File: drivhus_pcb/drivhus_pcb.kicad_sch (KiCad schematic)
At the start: 10 parts, among them J1 Setup, J2 Conn_01x19_Female, J3 Conn_01x19_Female, J4 Conn_01x04_Male, J5 Conn_Coaxial_Power, J6 +12V, J7 -12V, J8 +5V, J9 -5V, U1 SP3485EN

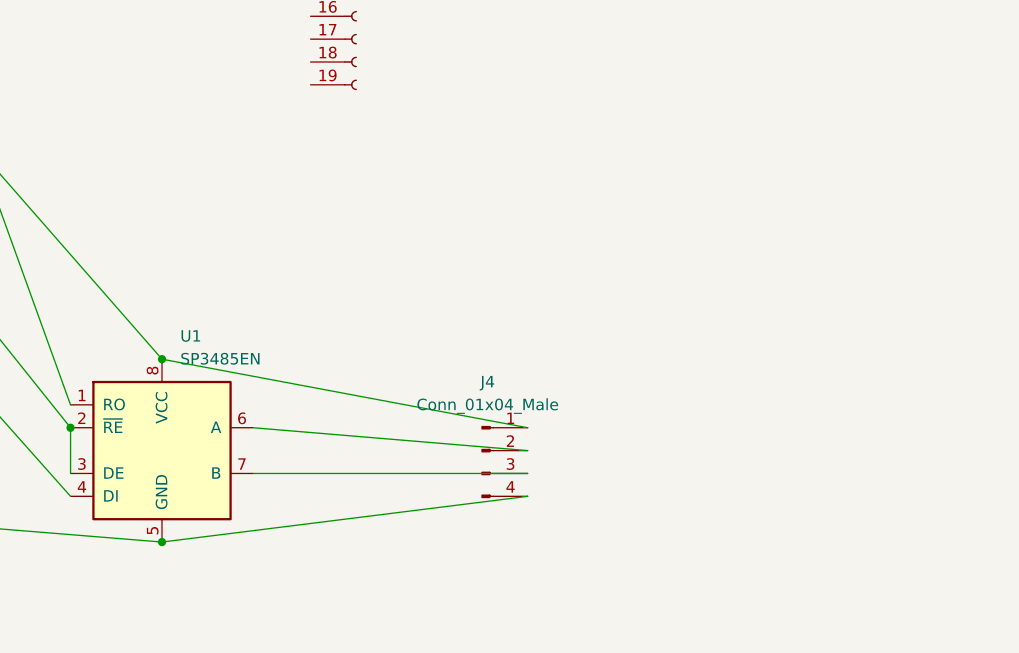
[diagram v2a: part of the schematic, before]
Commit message: Use RJ45 as quick-connect for RS-485 bus. Two connectors, so controller can be in the middle of bus
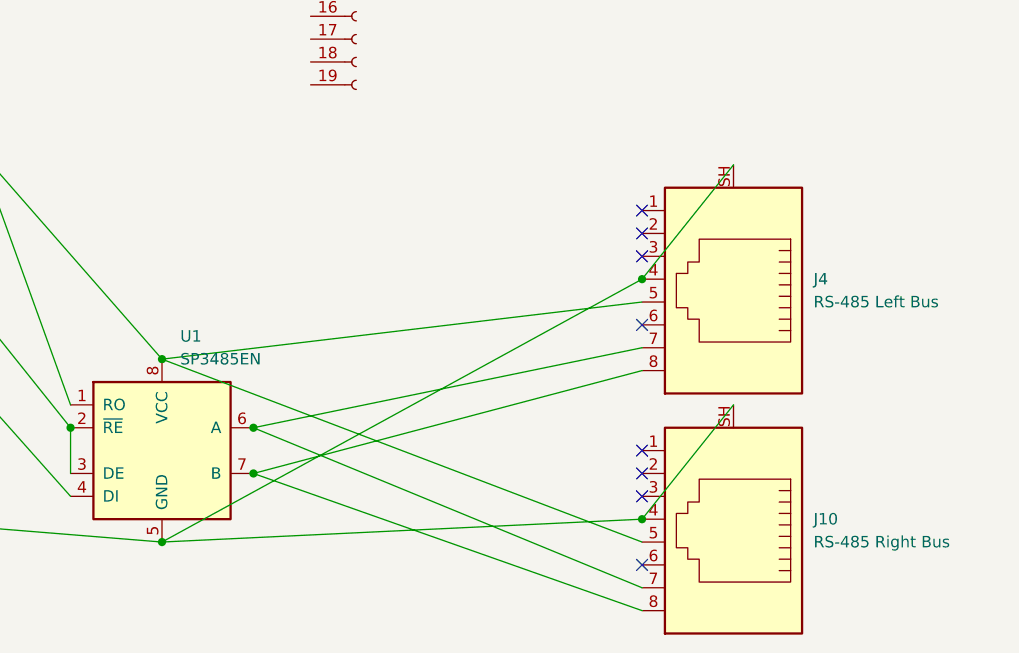
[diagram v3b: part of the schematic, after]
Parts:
- removed J4: Conn_01x04_Male, TerminalBlock:TerminalBlock_bornier-4_P5.08mm, symbol Connector:Conn_01x04_Male
- added J10: RS-485 Right Bus, Connector_RJ:RJ45_Ninigi_GE, symbol Connector:RJ45_Shielded
- added J4: RS-485 Left Bus, Connector_RJ:RJ45_Ninigi_GE, symbol Connector:RJ45_Shielded
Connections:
- net +5V: now also J10.5, J4.5
- net GND: now also J10.4, J10.SH, J4.4, J4.SH
- net at U1.6 (A): now also J10.7, J4.7
- net at U1.7 (B): now also J10.8, J4.8
- no-connect marks 0 -> 8
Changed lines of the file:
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@@
 (kicad_sch (version 20211123) (generator eeschema)
   (paper "A4")
+  (junction (at 179.07 156.21) (diameter 0) (color 0 0 0 0)
+  )
+  (junction (at 68.58 48.26) (diameter 0) (color 0 0 0 0)
+  )
+  (junction (at 44.45 33.02) (diameter 0) (color 0 0 0 0)
+  )
+  (junction (at 44.45 45.72) (diameter 0) (color 0 0 0 0)
+  )
   (junction (at 125.73 158.75) (diameter 0) (color 0 0 0 0)
   )
-  (junction (at 68.58 48.26) (diameter 0) (color 0 0 0 0)
-  )
-  (junction (at 44.45 33.02) (diameter 0) (color 0 0 0 0)
-  )
-  (junction (at 44.45 45.72) (diameter 0) (color 0 0 0 0)
+  (junction (at 135.89 151.13) (diameter 0) (color 0 0 0 0)
+  )
+  (junction (at 179.07 129.54) (diameter 0) (color 0 0 0 0)
   )
   (junction (at 99.06 107.95) (diameter 0) (color 0 0 0 0)
   )
+  (junction (at 135.89 146.05) (diameter 0) (color 0 0 0 0)
+  )
+  (junction (at 68.58 33.02) (diameter 0) (color 0 0 0 0)
+  )
   (junction (at 125.73 138.43) (diameter 0) (color 0 0 0 0)
   )
-  (junction (at 68.58 33.02) (diameter 0) (color 0 0 0 0)
-  )
   (junction (at 115.57 146.05) (diameter 0) (color 0 0 0 0)
   )
   (junction (at 99.06 95.25) (diameter 0) (color 0 0 0 0)
   )
+  (no_connect (at 179.07 148.59))
+  (no_connect (at 179.07 121.92))
+  (no_connect (at 179.07 153.67))
+  (no_connect (at 179.07 124.46))
+  (no_connect (at 179.07 134.62))
+  (no_connect (at 179.07 127))
+  (no_connect (at 179.07 151.13))
+  (no_connect (at 179.07 161.29))
+  (wire (pts (xy 135.89 146.05) (xy 179.07 163.83))
+    (stroke (width 0) (type default) (color 0 0 0 0))
+  )
   (wire (pts (xy 78.74 154.94) (xy 125.73 158.75))
     (stroke (width 0) (type default) (color 0 0 0 0))
@@
     (stroke (width 0) (type default) (color 0 0 0 0))
   )
+  (wire (pts (xy 179.07 156.21) (xy 189.23 143.51))
+    (stroke (width 0) (type default) (color 0 0 0 0))
+  )
+  (wire (pts (xy 179.07 129.54) (xy 189.23 116.84))
+    (stroke (width 0) (type default) (color 0 0 0 0))
+  )
   (wire (pts (xy 25.4 33.02) (xy 44.45 33.02))
     (stroke (width 0) (type default) (color 0 0 0 0))
@@
     (stroke (width 0) (type default) (color 0 0 0 0))
   )
+  (wire (pts (xy 125.73 158.75) (xy 179.07 156.21))
+    (stroke (width 0) (type default) (color 0 0 0 0))
+  )
+  (wire (pts (xy 135.89 146.05) (xy 179.07 137.16))
+    (stroke (width 0) (type default) (color 0 0 0 0))
+  )
   (wire (pts (xy 85.09 119.38) (xy 115.57 153.67))
     (stroke (width 0) (type default) (color 0 0 0 0))
   )
-  (wire (pts (xy 135.89 146.05) (xy 166.37 148.59))
-    (stroke (width 0) (type default) (color 0 0 0 0))
-  )
   (wire (pts (xy 99.06 95.25) (xy 78.74 154.94))
     (stroke (width 0) (type default) (color 0 0 0 0))
@@
     (stroke (width 0) (type default) (color 0 0 0 0))
   )
+  (wire (pts (xy 135.89 151.13) (xy 179.07 139.7))
+    (stroke (width 0) (type default) (color 0 0 0 0))
+  )
   (wire (pts (xy 99.06 95.25) (xy 55.88 80.01))
     (stroke (width 0) (type default) (color 0 0 0 0))
@@
     (stroke (width 0) (type default) (color 0 0 0 0))
   )
-  (wire (pts (xy 135.89 151.13) (xy 166.37 151.13))
+  (wire (pts (xy 125.73 138.43) (xy 179.07 158.75))
+    (stroke (width 0) (type default) (color 0 0 0 0))
+  )
+  (wire (pts (xy 125.73 138.43) (xy 179.07 132.08))
     (stroke (width 0) (type default) (color 0 0 0 0))
   )
@@
     (stroke (width 0) (type default) (color 0 0 0 0))
   )
-  (wire (pts (xy 166.37 153.67) (xy 125.73 158.75))
+  (wire (pts (xy 135.89 151.13) (xy 179.07 166.37))
     (stroke (width 0) (type default) (color 0 0 0 0))
   )
@@
     (stroke (width 0) (type default) (color 0 0 0 0))
   )
-  (wire (pts (xy 166.37 146.05) (xy 125.73 138.43))
+  (wire (pts (xy 125.73 158.75) (xy 179.07 129.54))
     (stroke (width 0) (type default) (color 0 0 0 0))
   )
@@
   (symbol (lib_id "power:GND") (at 68.58 48.26 90) (unit 1)
     (in_bom yes) (on_board yes) (fields_autoplaced)
-    (property "Reference" "#PWR?" (id 0) (at 74.93 48.26 0)
+    (property "Reference" "#PWR02" (id 0) (at 74.93 48.26 0)
       (effects (font (size 1.27 1.27)) hide)
     )
@@
   (symbol (lib_id "power:+5V") (at 68.58 33.02 270) (unit 1)
     (in_bom yes) (on_board yes) (fields_autoplaced)
-    (property "Reference" "#PWR?" (id 0) (at 64.77 33.02 0)
+    (property "Reference" "#PWR01" (id 0) (at 64.77 33.02 0)
       (effects (font (size 1.27 1.27)) hide)
     )
@@
   (symbol (lib_id "power:PWR_FLAG") (at 68.58 33.02 270) (unit 1)
     (in_bom yes) (on_board yes) (fields_autoplaced)
-    (property "Reference" "#FLG?" (id 0) (at 70.485 33.02 0)
+    (property "Reference" "#FLG01" (id 0) (at 70.485 33.02 0)
       (effects (font (size 1.27 1.27)) hide)
     )
@@
     )
     (pin "1")
+  )
+  (symbol (lib_id "Connector:RJ45_Shielded") (at 189.23 156.21 180) (unit 1)
+    (in_bom yes) (on_board yes) (fields_autoplaced)
+    (property "Reference" "J10" (id 0) (at 198.12 156.2099 0)
+      (effects (font (size 1.27 1.27)) (justify right))
+    )
+    (property "Value" "RS-485 Right Bus" (id 1) (at 198.12 158.7499 0)
+      (effects (font (size 1.27 1.27)) (justify right))
+    )
+    (property "Footprint" "Connector_RJ:RJ45_Ninigi_GE" (id 2) (at 189.23 156.845 90)
+      (effects (font (size 1.27 1.27)) hide)
+    )
+    (property "Datasheet" "~" (id 3) (at 189.23 156.845 90)
+      (effects (font (size 1.27 1.27)) hide)
+    )
+    (pin "1")
+    (pin "2")
+    (pin "3")
+    (pin "4")
+    (pin "5")
+    (pin "6")
+    (pin "7")
+    (pin "8")
+    (pin "SH")
+  )
+  (symbol (lib_id "Connector:RJ45_Shielded") (at 189.23 129.54 180) (unit 1)
+    (in_bom yes) (on_board yes) (fields_autoplaced)
+    (property "Reference" "J4" (id 0) (at 198.12 129.5399 0)
+      (effects (font (size 1.27 1.27)) (justify right))
+    )
+    (property "Value" "RS-485 Left Bus" (id 1) (at 198.12 132.0799 0)
+      (effects (font (size 1.27 1.27)) (justify right))
+    )
+    (property "Footprint" "Connector_RJ:RJ45_Ninigi_GE" (id 2) (at 189.23 130.175 90)
+      (effects (font (size 1.27 1.27)) hide)
+    )
+    (property "Datasheet" "~" (id 3) (at 189.23 130.175 90)
+      (effects (font (size 1.27 1.27)) hide)
+    )
+    (pin "1")
+    (pin "2")
+    (pin "3")
+    (pin "4")
+    (pin "5")
+    (pin "6")
+    (pin "7")
+    (pin "8")
+    (pin "SH")
   )
   (symbol (lib_id "Connector:Conn_Coaxial_Power") (at 25.4 35.56 0) (unit 1)
@@
     (pin "9")
   )
-  (symbol (lib_id "Connector:Conn_01x04_Male") (at 161.29 148.59 0) (unit 1)
-    (in_bom yes) (on_board yes) (fields_autoplaced)
-    (property "Reference" "J4" (id 0) (at 161.925 140.97 0))
-    (property "Value" "Conn_01x04_Male" (id 1) (at 161.925 143.51 0))
-    (property "Footprint" "TerminalBlock:TerminalBlock_bornier-4_P5.08mm" (id 2) (at 161.29 148.59 0)
-      (effects (font (size 1.27 1.27)) hide)
-    )
-    (property "Datasheet" "~" (id 3) (at 161.29 148.59 0)
-      (effects (font (size 1.27 1.27)) hide)
-    )
-    (pin "1")
-    (pin "2")
-    (pin "3")
-    (pin "4")
-  )
   (symbol (lib_id "Connector:Conn_01x02_Male") (at 39.37 45.72 0) (unit 1)
     (in_bom yes) (on_board yes) (fields_autoplaced)
@@
   (symbol (lib_id "power:PWR_FLAG") (at 68.58 48.26 270) (unit 1)
     (in_bom yes) (on_board yes) (fields_autoplaced)
-    (property "Reference" "#FLG?" (id 0) (at 70.485 48.26 0)
+    (property "Reference" "#FLG02" (id 0) (at 70.485 48.26 0)
       (effects (font (size 1.27 1.27)) hide)
     )
@@
   (symbol_instances
     (path "/6684c32e-3803-4319-8b63-ec9f51a3684f"
-      (reference "#FLG?") (unit 1) (value "PWR_FLAG") (footprint "")
+      (reference "#FLG01") (unit 1) (value "PWR_FLAG") (footprint "")
     )
     (path "/afd29fb3-3a65-4217-9226-773dc2d8f59e"
-      (reference "#FLG?") (unit 1) (value "PWR_FLAG") (footprint "")
+      (reference "#FLG02") (unit 1) (value "PWR_FLAG") (footprint "")
+    )
+    (path "/535aed7a-9a8f-4e34-9373-af5cf64d5139"
+      (reference "#PWR01") (unit 1) (value "+5V") (footprint "")
     )
     (path "/19242a02-819d-4624-9ccb-e3ac0e9ec204"
-      (reference "#PWR?") (unit 1) (value "GND") (footprint "")
-    )
-    (path "/535aed7a-9a8f-4e34-9373-af5cf64d5139"
-      (reference "#PWR?") (unit 1) (value "+5V") (footprint "")
+      (reference "#PWR02") (unit 1) (value "GND") (footprint "")
     )
     (path "/cc1d9e72-6d7e-4b1a-895f-9e83cfa7ed74"
@@
       (reference "J3") (unit 1) (value "Conn_01x19_Female") (footprint "Connector_PinHeader_2.54mm:PinHeader_1x19_P2.54mm_Vertical")
     )
-    (path "/76df43cb-8047-4fdb-b097-721514b7aec0"
-      (reference "J4") (unit 1) (value "Conn_01x04_Male") (footprint "TerminalBlock:TerminalBlock_bornier-4_P5.08mm")
+    (path "/6e56a961-2194-4532-a3e5-f67215cce47a"
+      (reference "J4") (unit 1) (value "RS-485 Left Bus") (footprint "Connector_RJ:RJ45_Ninigi_GE")
     )
     (path "/7004177e-6516-4f66-9094-c96ea91df607"
@@
       (reference "J9") (unit 1) (value "-5V") (footprint "Connector_PinHeader_2.54mm:PinHeader_1x02_P2.54mm_Vertical")
     )
+    (path "/68f235f1-7035-4dc2-922d-a436236980a5"
+      (reference "J10") (unit 1) (value "RS-485 Right Bus") (footprint "Connector_RJ:RJ45_Ninigi_GE")
+    )
     (path "/ba1d673c-507b-434f-9d3f-83c44effc345"

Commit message: Added voltage sensor (max 14.5V)
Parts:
- added R1: 1M, Resistor_SMD:R_1206_3216Metric, symbol Device:R
- added R2: 300K, Resistor_SMD:R_1206_3216Metric, symbol Device:R
- J1: footprint Connector_PinHeader_2.54mm:PinHeader_1x02_P2.54mm_Vertical -> Resistor_SMD:R_1206_3216Metric
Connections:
- net at J2.5 (Pin_5): now also R1.2, R2.1
- net at J5.1 (In), J6.1 (Pin_1), J6.2 (Pin_2): now also R1.1
- net at J5.2 (Ext), J7.1 (Pin_1), J7.2 (Pin_2): now also R2.2
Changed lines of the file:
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@@
   (junction (at 99.06 107.95) (diameter 0) (color 0 0 0 0)
+  )
+  (junction (at 27.94 64.77) (diameter 0) (color 0 0 0 0)
   )
   (junction (at 135.89 146.05) (diameter 0) (color 0 0 0 0)
@@
     (stroke (width 0) (type default) (color 0 0 0 0))
   )
+  (wire (pts (xy 99.06 72.39) (xy 27.94 64.77))
+    (stroke (width 0) (type default) (color 0 0 0 0))
+  )
+  (wire (pts (xy 27.94 76.2) (xy 44.45 45.72))
+    (stroke (width 0) (type default) (color 0 0 0 0))
+  )
   (wire (pts (xy 25.4 33.02) (xy 44.45 33.02))
     (stroke (width 0) (type default) (color 0 0 0 0))
@@
     (stroke (width 0) (type default) (color 0 0 0 0))
   )
+  (wire (pts (xy 27.94 64.77) (xy 27.94 68.58))
+    (stroke (width 0) (type default) (color 0 0 0 0))
+  )
   (wire (pts (xy 115.57 146.05) (xy 115.57 151.13))
     (stroke (width 0) (type default) (color 0 0 0 0))
@@
   )
   (wire (pts (xy 25.4 40.64) (xy 44.45 45.72))
+    (stroke (width 0) (type default) (color 0 0 0 0))
+  )
+  (wire (pts (xy 44.45 33.02) (xy 27.94 57.15))
     (stroke (width 0) (type default) (color 0 0 0 0))
   )
@@
     (pin "1")
   )
+  (symbol (lib_id "Device:R") (at 27.94 60.96 0) (unit 1)
+    (in_bom yes) (on_board yes) (fields_autoplaced)
+    (property "Reference" "R1" (id 0) (at 30.48 59.6899 0)
+      (effects (font (size 1.27 1.27)) (justify left))
+    )
+    (property "Value" "1M" (id 1) (at 30.48 62.2299 0)
+      (effects (font (size 1.27 1.27)) (justify left))
+    )
+    (property "Footprint" "Resistor_SMD:R_1206_3216Metric" (id 2) (at 26.162 60.96 90)
+      (effects (font (size 1.27 1.27)) hide)
+    )
+    (property "Datasheet" "~" (id 3) (at 27.94 60.96 0)
+      (effects (font (size 1.27 1.27)) hide)
+    )
+    (pin "1")
+    (pin "2")
+  )
   (symbol (lib_id "power:PWR_FLAG") (at 68.58 33.02 270) (unit 1)
     (in_bom yes) (on_board yes) (fields_autoplaced)
@@
     (pin "2")
   )
+  (symbol (lib_id "Device:R") (at 27.94 72.39 0) (unit 1)
+    (in_bom yes) (on_board yes) (fields_autoplaced)
+    (property "Reference" "R2" (id 0) (at 30.48 71.1199 0)
+      (effects (font (size 1.27 1.27)) (justify left))
+    )
+    (property "Value" "300K" (id 1) (at 30.48 73.6599 0)
+      (effects (font (size 1.27 1.27)) (justify left))
+    )
+    (property "Footprint" "Resistor_SMD:R_1206_3216Metric" (id 2) (at 26.162 72.39 90)
+      (effects (font (size 1.27 1.27)) hide)
+    )
+    (property "Datasheet" "~" (id 3) (at 27.94 72.39 0)
+      (effects (font (size 1.27 1.27)) hide)
+    )
+    (pin "1")
+    (pin "2")
+  )
   (symbol (lib_id "Interface_UART:SP3485EN") (at 125.73 148.59 0) (unit 1)
     (in_bom yes) (on_board yes) (fields_autoplaced)
@@
     (property "Reference" "J1" (id 0) (at 51.435 72.39 0))
     (property "Value" "Setup" (id 1) (at 51.435 74.93 0))
-    (property "Footprint" "Connector_PinHeader_2.54mm:PinHeader_1x02_P2.54mm_Vertical" (id 2) (at 50.8 77.47 0)
+    (property "Footprint" "Resistor_SMD:R_1206_3216Metric" (id 2) (at 50.8 77.47 0)
       (effects (font (size 1.27 1.27)) hide)
     )
@@
     )
     (path "/cc1d9e72-6d7e-4b1a-895f-9e83cfa7ed74"
-      (reference "J1") (unit 1) (value "Setup") (footprint "Connector_PinHeader_2.54mm:PinHeader_1x02_P2.54mm_Vertical")
+      (reference "J1") (unit 1) (value "Setup") (footprint "Resistor_SMD:R_1206_3216Metric")
     )
     (path "/2d5cde52-f66b-4d74-a993-25971513d148"
@@
       (reference "J10") (unit 1) (value "RS-485 Right Bus") (footprint "Connector_RJ:RJ45_Ninigi_GE")
     )
+    (path "/57442f99-2d46-4e71-bd92-43296b060c85"
+      (reference "R1") (unit 1) (value "1M") (footprint "Resistor_SMD:R_1206_3216Metric")
+    )
+    (path "/b9829576-80da-4f5b-89ea-8f9c0d53d78f"
+      (reference "R2") (unit 1) (value "300K") (footprint "Resistor_SMD:R_1206_3216Metric")
+    )
     (path "/ba1d673c-507b-434f-9d3f-83c44effc345"
